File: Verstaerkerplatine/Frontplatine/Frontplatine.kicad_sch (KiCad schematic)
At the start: 38 parts, among them J1 GND, J10 IV_IN_+, J11 IV_OUT, J12 IV_REF, J13 AVS_IN_+, J14 AVS_IN_-, J16 A0, J17 A1, J18 A2, J19 A3, J20 GND, J21 -5V, J22 3.3V, J23 5V, J24 DI_IN_2, J25 DI_IN_1, J26 DI_OUT_3, J27 DI_OUT_2, J28 DI_OUT_1, J29 EM_20, J3 EM_OUT, J30 LED_20, J31 D/A_+, J32 5V_BUS, J33 3.3V_BUS, J34 EM_KOND, J4 GND_EM, J5 EM_IN, J6 PW_IN, J7 PW_OUT, J8 REF, J9 IV_IN_-

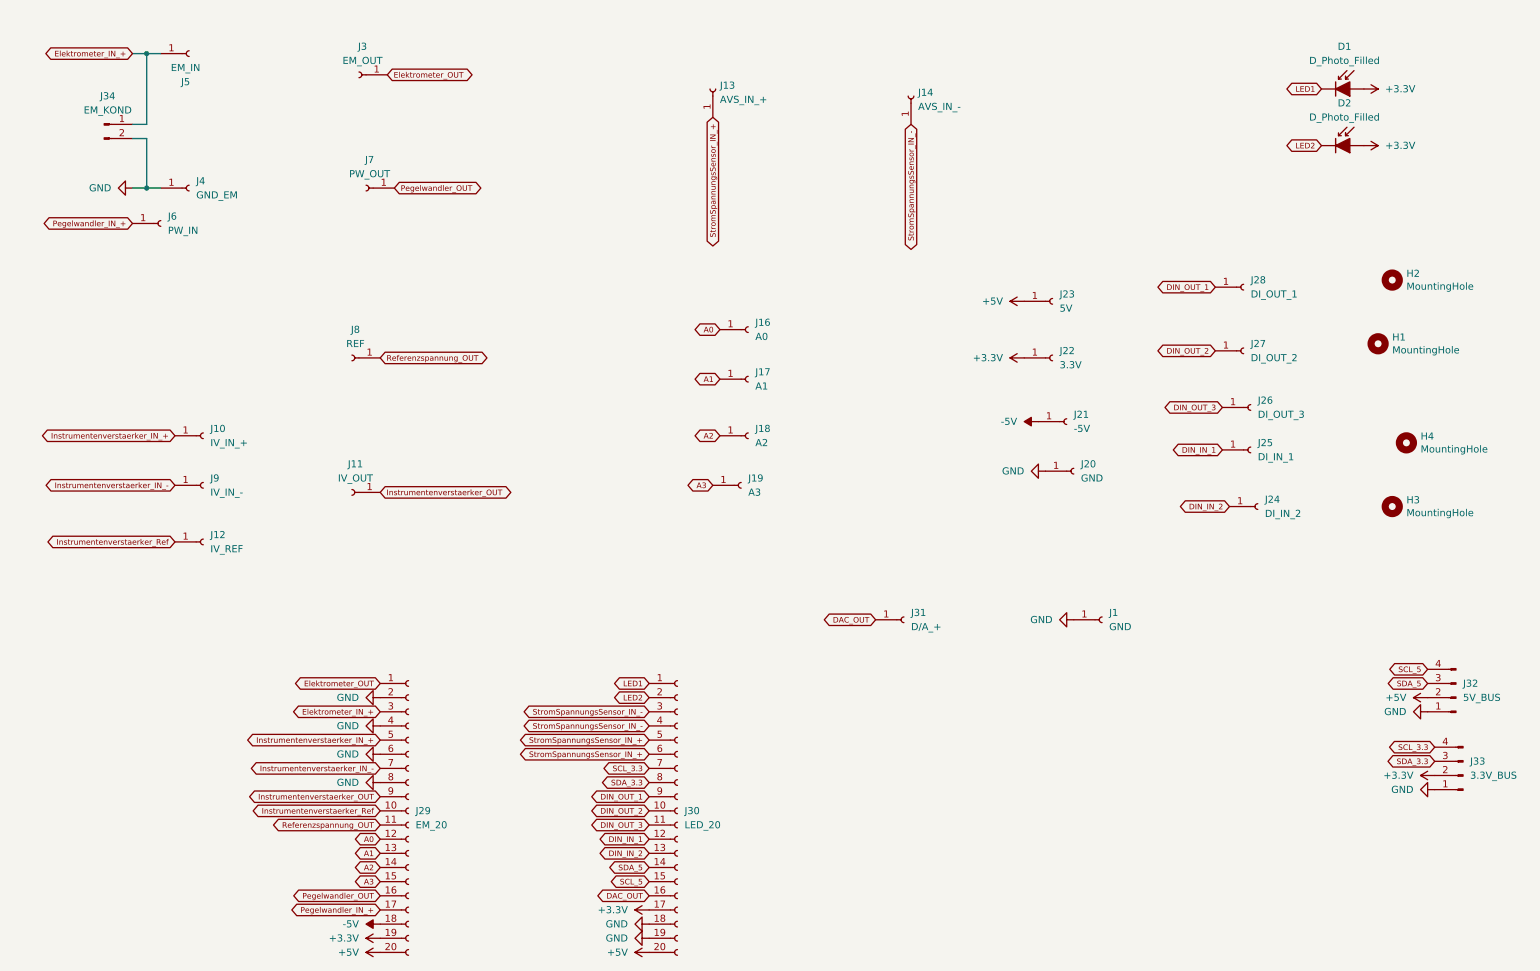
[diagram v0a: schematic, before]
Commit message: wired connection for CA3140 in and IN219 IN+ and IN-
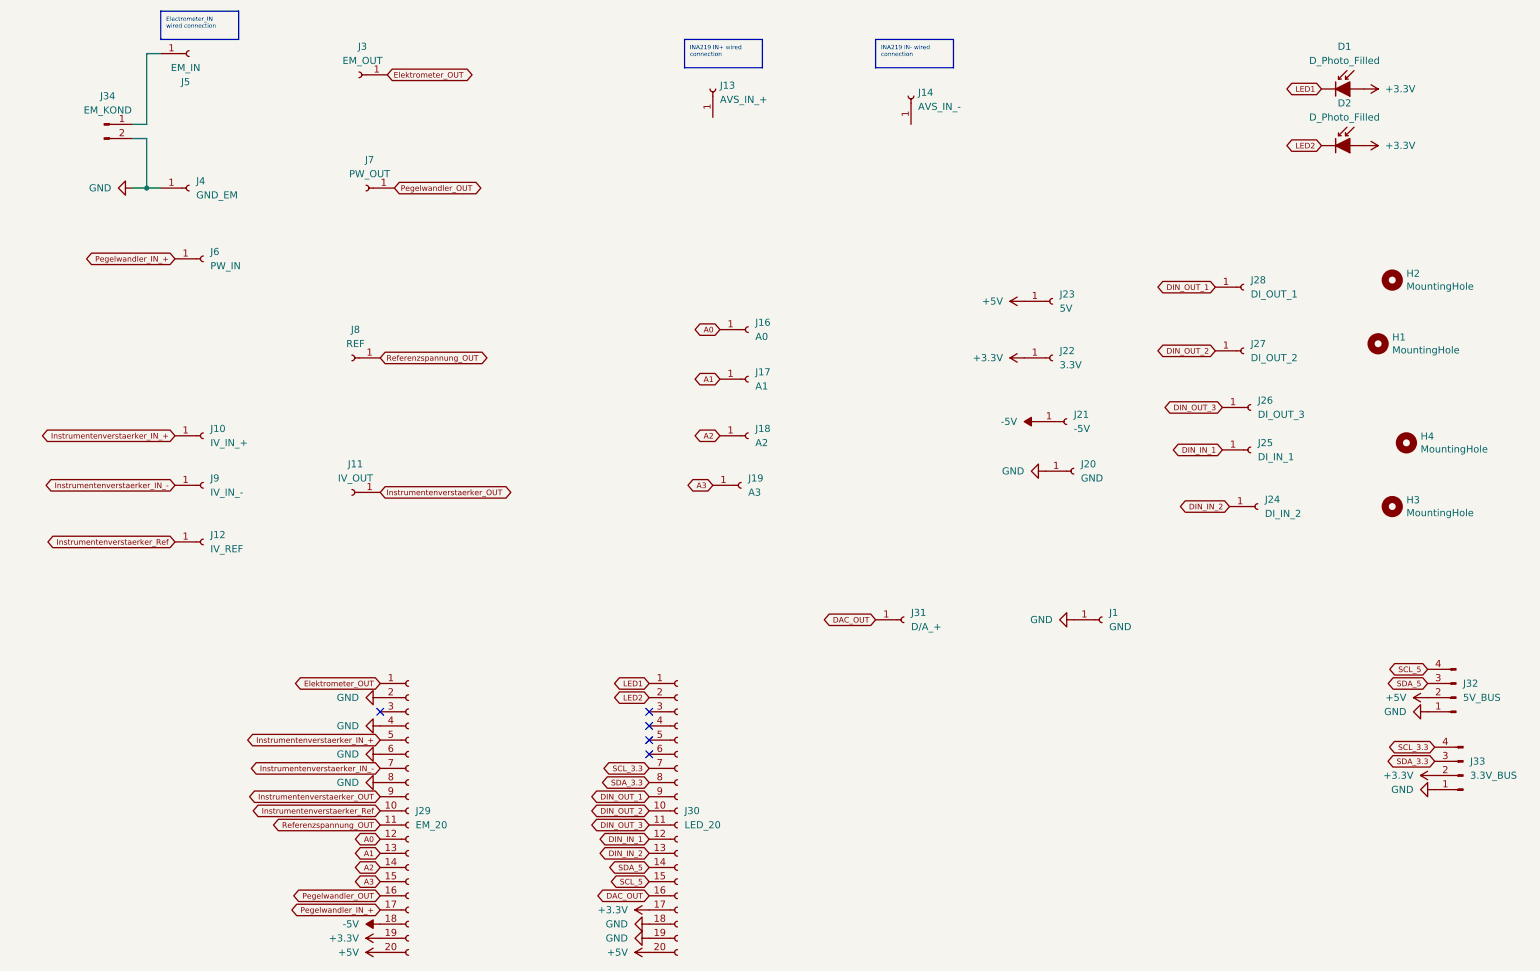
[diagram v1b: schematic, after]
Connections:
- net Elektrometer_IN_+: no longer names the net of J34.1 (Pin_1), J5.1 (Pin_1)
- net Elektrometer_IN_+: no longer J29.3 (Pin_3)
- removed net StromSpannungsSensor_IN_+: J13.1 (Pin_1), J30.5 (Pin_5), J30.6 (Pin_6)
- removed net StromSpannungsSensor_IN_-: J14.1 (Pin_1), J30.3 (Pin_3), J30.4 (Pin_4)
- no-connect marks 0 -> 5
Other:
- moved on the sheet: J6
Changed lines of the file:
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@@
 	(generator_version "9.0")
 	(paper "A4")
-	(junction
-		(at 35.56 29.21)
-		(diameter 0)
-		(color 0 0 0 0)
+	(text_box "INA219 IN+ wired connection\n"
+		(exclude_from_sim no)
+		(at 132.08 26.67 0)
+		(size 13.97 5.08)
+		(margins 0.9525 0.9525 0.9525 0.9525)
+		(stroke
+			(width 0)
+			(type solid)
+		)
+		(fill
+			(type none)
+		)
+		(effects
+			(font
+				(size 0.762 0.762)
+			)
+			(justify left top)
+		)
+	)
+	(text_box "Electrometer_IN wired connection\n"
+		(exclude_from_sim no)
+		(at 38.1 21.59 0)
+		(size 13.97 5.08)
+		(margins 0.9525 0.9525 0.9525 0.9525)
+		(stroke
+			(width 0)
+			(type solid)
+		)
+		(fill
+			(type none)
+		)
+		(effects
+			(font
+				(size 0.762 0.762)
+			)
+			(justify left top)
+		)
+	)
+	(text_box "INA219 IN- wired connection\n"
+		(exclude_from_sim no)
+		(at 166.37 26.67 0)
+		(size 13.97 5.08)
+		(margins 0.9525 0.9525 0.9525 0.9525)
+		(stroke
+			(width 0)
+			(type solid)
+		)
+		(fill
+			(type none)
+		)
+		(effects
+			(font
+				(size 0.762 0.762)
+			)
+			(justify left top)
+		)
 	)
 	(junction
@@
 		(color 0 0 0 0)
 	)
-	(wire
-		(pts
-			(xy 33.02 44.45) (xy 35.56 44.45)
-		)
-		(stroke
-			(width 0)
-			(type default)
-		)
+	(no_connect
+		(at 125.73 154.94)
+	)
+	(no_connect
+		(at 77.47 147.32)
+	)
+	(no_connect
+		(at 125.73 147.32)
+	)
+	(no_connect
+		(at 125.73 149.86)
+	)
+	(no_connect
+		(at 125.73 152.4)
 	)
 	(wire
 		(pts
-			(xy 35.56 29.21) (xy 33.02 29.21)
+			(xy 33.02 44.45) (xy 35.56 44.45)
 		)
 		(stroke
@@
 		)
 	)
-	(global_label "StromSpannungsSensor_IN_-"
-		(shape bidirectional)
-		(at 172.72 41.91 270)
-		(fields_autoplaced yes)
-		(effects
-			(font
-				(size 1 1)
-			)
-			(justify right)
-		)
-		(property "Intersheetrefs" "${INTERSHEET_REFS}"
-			(at 172.72 66.945 90)
-			(effects
-				(font
-					(size 1.27 1.27)
-				)
-				(justify right)
-				(hide yes)
-			)
-		)
-	)
 	(global_label "Instrumentenverstaerker_IN_-"
 		(shape bidirectional)
@@
 		)
 	)
-	(global_label "StromSpannungsSensor_IN_-"
-		(shape bidirectional)
-		(at 125.73 149.86 180)
-		(fields_autoplaced yes)
-		(effects
-			(font
-				(size 1 1)
-			)
-			(justify right)
-		)
-		(property "Intersheetrefs" "${INTERSHEET_REFS}"
-			(at 101.335 149.86 0)
-			(effects
-				(font
-					(size 1.27 1.27)
-				)
-				(justify right)
-				(hide yes)
-			)
-		)
-	)
 	(global_label "DIN_IN_1"
 		(shape bidirectional)
@@
 		)
 	)
-	(global_label "StromSpannungsSensor_IN_+"
-		(shape bidirectional)
-		(at 125.73 154.94 180)
-		(fields_autoplaced yes)
-		(effects
-			(font
-				(size 1 1)
-			)
-			(justify right)
-		)
-		(property "Intersheetrefs" "${INTERSHEET_REFS}"
-			(at 101.335 154.94 0)
-			(effects
-				(font
-					(size 1.27 1.27)
-				)
-				(justify right)
-				(hide yes)
-			)
-		)
-	)
 	(global_label "A1"
 		(shape bidirectional)
@@
 	(global_label "Pegelwandler_IN_+"
 		(shape bidirectional)
-		(at 33.02 59.69 180)
+		(at 40.64 66.04 180)
 		(fields_autoplaced yes)
 		(effects
@@
 		)
 		(property "Intersheetrefs" "${INTERSHEET_REFS}"
-			(at 16.2443 59.69 0)
+			(at 23.8643 66.04 0)
 			(effects
 				(font
@@
 		)
 	)
-	(global_label "Elektrometer_IN_+"
-		(shape bidirectional)
-		(at 77.47 147.32 180)
-		(fields_autoplaced yes)
-		(effects
-			(font
-				(size 1 1)
-			)
-			(justify right)
-		)
-		(property "Intersheetrefs" "${INTERSHEET_REFS}"
-			(at 61.1707 147.32 0)
-			(effects
-				(font
-					(size 1.27 1.27)
-				)
-				(justify right)
-				(hide yes)
-			)
-		)
-	)
 	(global_label "A0"
 		(shape bidirectional)
@@
 		)
 	)
-	(global_label "StromSpannungsSensor_IN_+"
-		(shape bidirectional)
-		(at 137.16 40.64 270)
-		(fields_autoplaced yes)
-		(effects
-			(font
-				(size 1 1)
-			)
-			(justify right)
-		)
-		(property "Intersheetrefs" "${INTERSHEET_REFS}"
-			(at 137.16 65.675 90)
-			(effects
-				(font
-					(size 1.27 1.27)
-				)
-				(justify right)
-				(hide yes)
-			)
-		)
-	)
 	(global_label "DIN_IN_1"
 		(shape bidirectional)
@@
 		)
 	)
-	(global_label "Elektrometer_IN_+"
-		(shape bidirectional)
-		(at 33.02 29.21 180)
-		(fields_autoplaced yes)
-		(effects
-			(font
-				(size 1 1)
-			)
-			(justify right)
-		)
-		(property "Intersheetrefs" "${INTERSHEET_REFS}"
-			(at 16.7207 29.21 0)
-			(effects
-				(font
-					(size 1.27 1.27)
-				)
-				(justify right)
-				(hide yes)
-			)
-		)
-	)
 	(global_label "DIN_OUT_3"
 		(shape bidirectional)
@@
 		)
 	)
-	(global_label "StromSpannungsSensor_IN_+"
-		(shape bidirectional)
-		(at 125.73 152.4 180)
-		(fields_autoplaced yes)
-		(effects
-			(font
-				(size 1 1)
-			)
-			(justify right)
-		)
-		(property "Intersheetrefs" "${INTERSHEET_REFS}"
-			(at 101.335 152.4 0)
-			(effects
-				(font
-					(size 1.27 1.27)
-				)
-				(justify right)
-				(hide yes)
-			)
-		)
-	)
 	(global_label "SCL_5"
 		(shape bidirectional)
@@
 		)
 	)
-	(global_label "StromSpannungsSensor_IN_-"
-		(shape bidirectional)
-		(at 125.73 147.32 180)
-		(fields_autoplaced yes)
-		(effects
-			(font
-				(size 1 1)
-			)
-			(justify right)
-		)
-		(property "Intersheetrefs" "${INTERSHEET_REFS}"
-			(at 101.335 147.32 0)
-			(effects
-				(font
-					(size 1.27 1.27)
-				)
-				(justify right)
-				(hide yes)
-			)
-		)
-	)
 	(global_label "DIN_OUT_1"
 		(shape bidirectional)
@@
 	(symbol
 		(lib_id "Connector:Conn_01x01_Socket")
-		(at 38.1 59.69 0)
+		(at 45.72 66.04 0)
 		(unit 1)
 		(exclude_from_sim no)
@@
 		(fields_autoplaced yes)
 		(property "Reference" "J6"
-			(at 39.37 58.42 0)
+			(at 46.99 64.77 0)
 			(effects
 				(font
@@
 		)
 		(property "Value" "PW_IN"
-			(at 39.37 60.96 0)
+			(at 46.99 67.31 0)
 			(effects
 				(font
@@
 		)
 		(property "Footprint" "Library_Frontplatine:MBU_1"
-			(at 38.1 59.69 0)
+			(at 45.72 66.04 0)
 			(effects
 				(font
@@
 		)
 		(property "Datasheet" "~"
-			(at 38.1 59.69 0)
+			(at 45.72 66.04 0)
 			(effects
 				(font
@@
 		)
 		(property "Description" ""
-			(at 38.1 59.69 0)
+			(at 45.72 66.04 0)
 			(effects
 				(font
